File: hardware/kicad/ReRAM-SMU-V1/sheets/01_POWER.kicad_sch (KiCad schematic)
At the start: 38 parts, among them J1 POWER_IN +-12V EXT 3.5mm pitc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, U1 LT3045EDD +5V_A 500mA 0.8uVrm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, U2 TLV1117-33 +3V3 800mA from +5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, U3 LTC6655BHMS8-5.0 DAC REF 5.0V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, U4 LTC6655BHMS8-2.5 ADC REF 2.5V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, U5 TPS3808G33 supervisor +3V3 Vt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

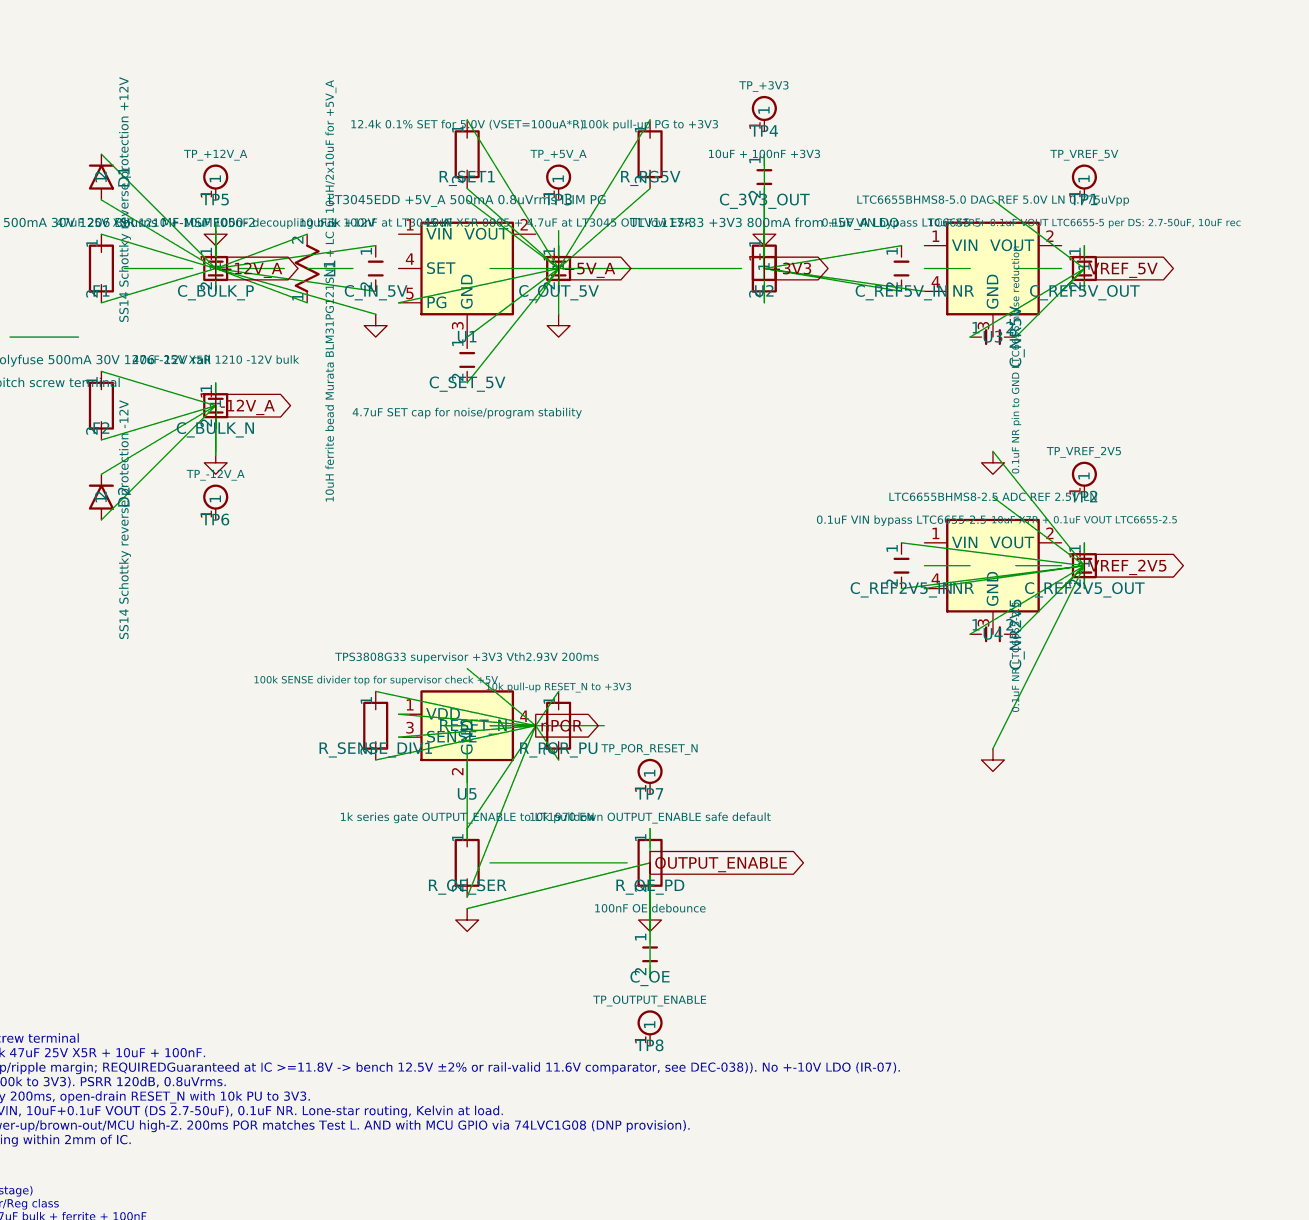
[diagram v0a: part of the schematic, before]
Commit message: style(kicad): re-serialize 01-06 + root to KiCad 9.0 schema 20250114 (formatting only)
- (version 20241014)->(version 20250114) + generator_version 10.0->9.0 on all 10 sch files including root + 01-04 verified via git diff
- lib_symbols block pretty-print expansion: property/symbol multi-line with explicit hide/exclude/effects font, no wire/symbol/net deletion
- 8 files: ReRAM-SMU-V1.kicad_pro (453+9-), ReRAM-SMU-V1.kicad_sch (806+53-), 01_POWER (5724+411-), 02_DAC (5816+436-), 03_OUTPUT (4308+276-), 04_KELVIN (3720+270-), 05_CURRENT_RANGES (375+217-), 06_ADC (492+452-); total 21694+2124-
- 07/08/09 excluded (already restored 184/236/156 lines, verified not truncated; no re-serialization needed)
- Functional audit: no net/junction/wire loss, netlist continuity preserved, ERC 124 headless (ca7eac3) unchanged by re-serialization
- Verified: wc -l 01 5739,02 5831,03 4322,04 3735,05 388,06 507,07 184,08 236,09 156
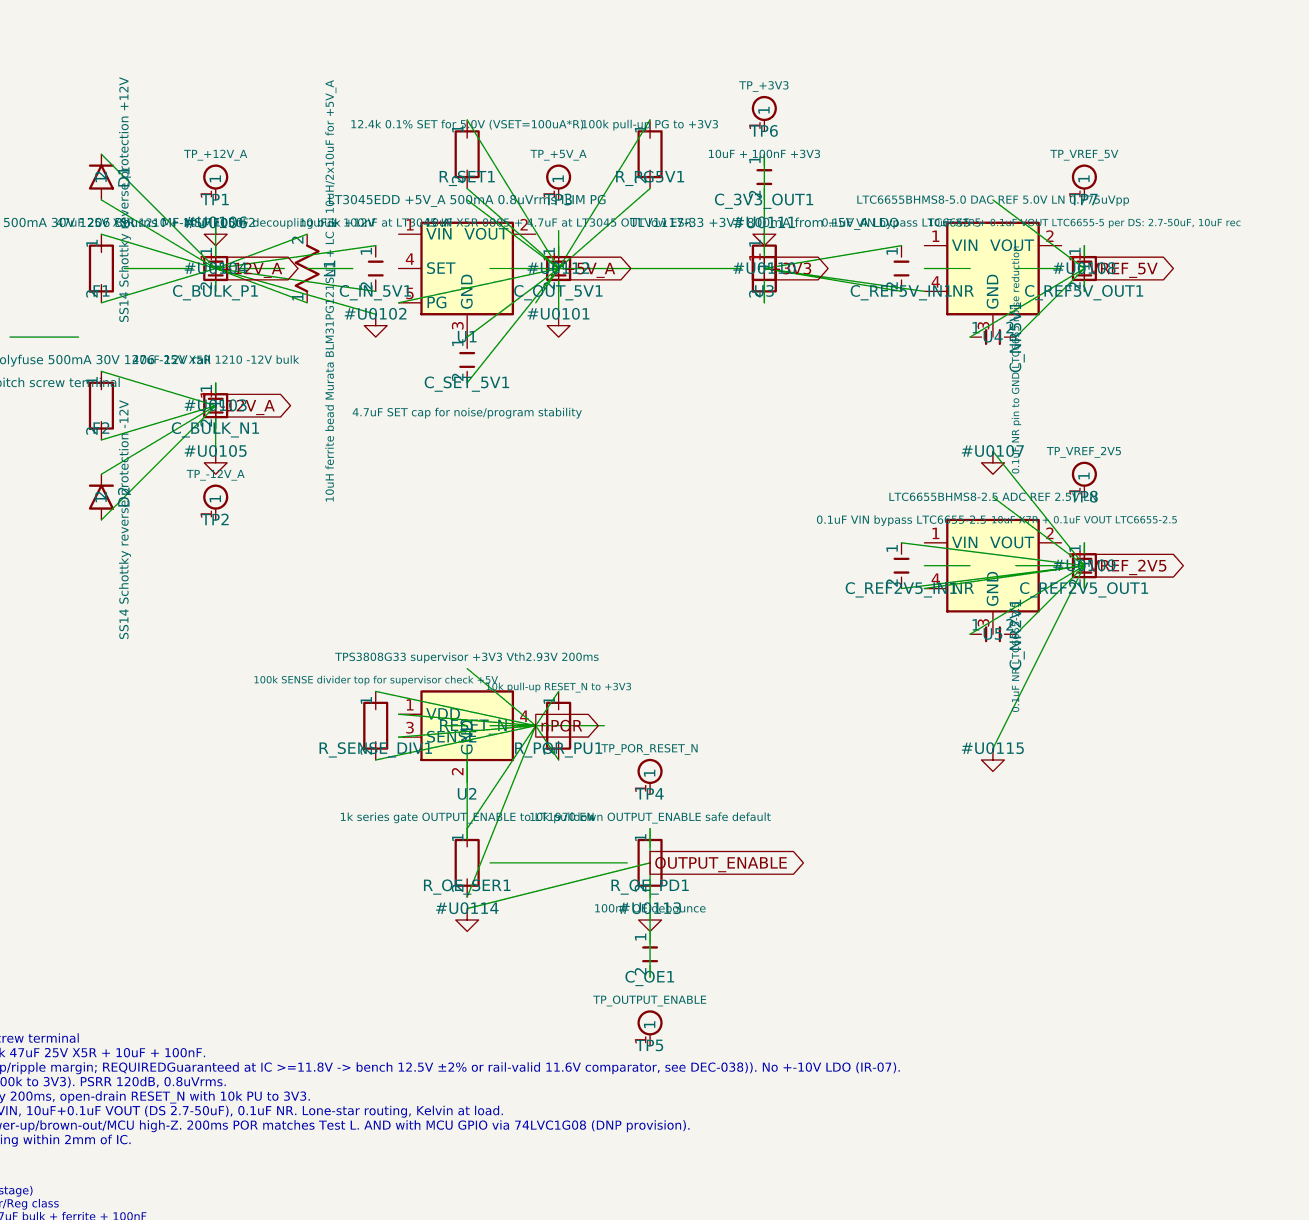
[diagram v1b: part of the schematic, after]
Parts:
- removed C_OE: 100nF OE debounce, Capacitor_SMD:C_0603_1608Metric, symbol Device:C
- removed R_OE_PD: 10k pulldown OUTPUT_ENABLE safe default, Resistor_SMD:R_0603_1608Metric, symbol Device:R
- removed R_OE_SER: 1k series gate OUTPUT_ENABLE to LT1970 EN, Resistor_SMD:R_0603_1608Metric, symbol Device:R
- removed R_POR_PU: 10k pull-up RESET_N to +3V3, Resistor_SMD:R_0603_1608Metric, symbol Device:R
- removed TP4: TP_+3V3, symbol ReRAM_SMU:TestPoint
- removed TP5: TP_+12V_A, symbol ReRAM_SMU:TestPoint
- removed U5: TPS3808G33 supervisor +3V3 Vth2.93V 200ms, Package_TO_SOT_SMD:SOT-23-6, symbol ReRAM_SMU:TPS3808
- added C_OE1: 100nF OE debounce, Capacitor_SMD:C_0603_1608Metric, symbol Device:C
- added R_OE_PD1: 10k pulldown OUTPUT_ENABLE safe default, Resistor_SMD:R_0603_1608Metric, symbol Device:R
- added R_OE_SER1: 1k series gate OUTPUT_ENABLE to LT1970 EN, Resistor_SMD:R_0603_1608Metric, symbol Device:R
- added R_POR_PU1: 10k pull-up RESET_N to +3V3, Resistor_SMD:R_0603_1608Metric, symbol Device:R
- added TP1: TP_+12V_A, symbol ReRAM_SMU:TestPoint
- added TP8: TP_VREF_2V5, symbol ReRAM_SMU:TestPoint
- added U2: TPS3808G33 supervisor +3V3 Vth2.93V 200ms, Package_TO_SOT_SMD:SOT-23-6, symbol ReRAM_SMU:TPS3808
- TP2: value TP_VREF_2V5 -> TP_-12V_A
- TP6: value TP_-12V_A -> TP_+3V3
- renumbered C_3V3_OUT to C_3V3_OUT1, C_BULK_N to C_BULK_N1, C_BULK_P to C_BULK_P1, C_IN_5V to C_IN_5V1, C_NR2V5 to C_NR2V1, C_NR5V to C_NR5V1, C_OUT_5V to C_OUT_5V1, C_REF2V5_IN to C_REF2V5_IN1, C_REF2V5_OUT to C_REF2V5_OUT1, C_REF5V_IN to C_REF5V_IN1, C_REF5V_OUT to C_REF5V_OUT1, C_SET_5V to C_SET_5V1, R_PG5V to R_PG5V1, TP7 to TP4, TP8 to TP5, TP1 to TP7, U2 to U3, U3 to U4, U4 to U5
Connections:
- net +12V_A: no longer C_BULK_P1.1
- net +3V3: no longer C_3V3_OUT1.2, U3.1
- net +5V_A: no longer C_OUT_5V1.1, C_OUT_5V1.2
- net -12V_A: no longer C_BULK_N1.2
- net OUTPUT_ENABLE: now also C_OE1.2, R_OE_PD1.1
- net nPOR: now also R_OE_SER1.1, R_OE_SER1.2, R_POR_PU1.1, R_POR_PU1.2, U2.1 (VDD), U2.3 (SENSE), U2.4 (RESET_N)
